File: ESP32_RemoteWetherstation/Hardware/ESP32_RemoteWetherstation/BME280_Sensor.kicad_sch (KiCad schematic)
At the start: 6 parts, among them U302 BME280

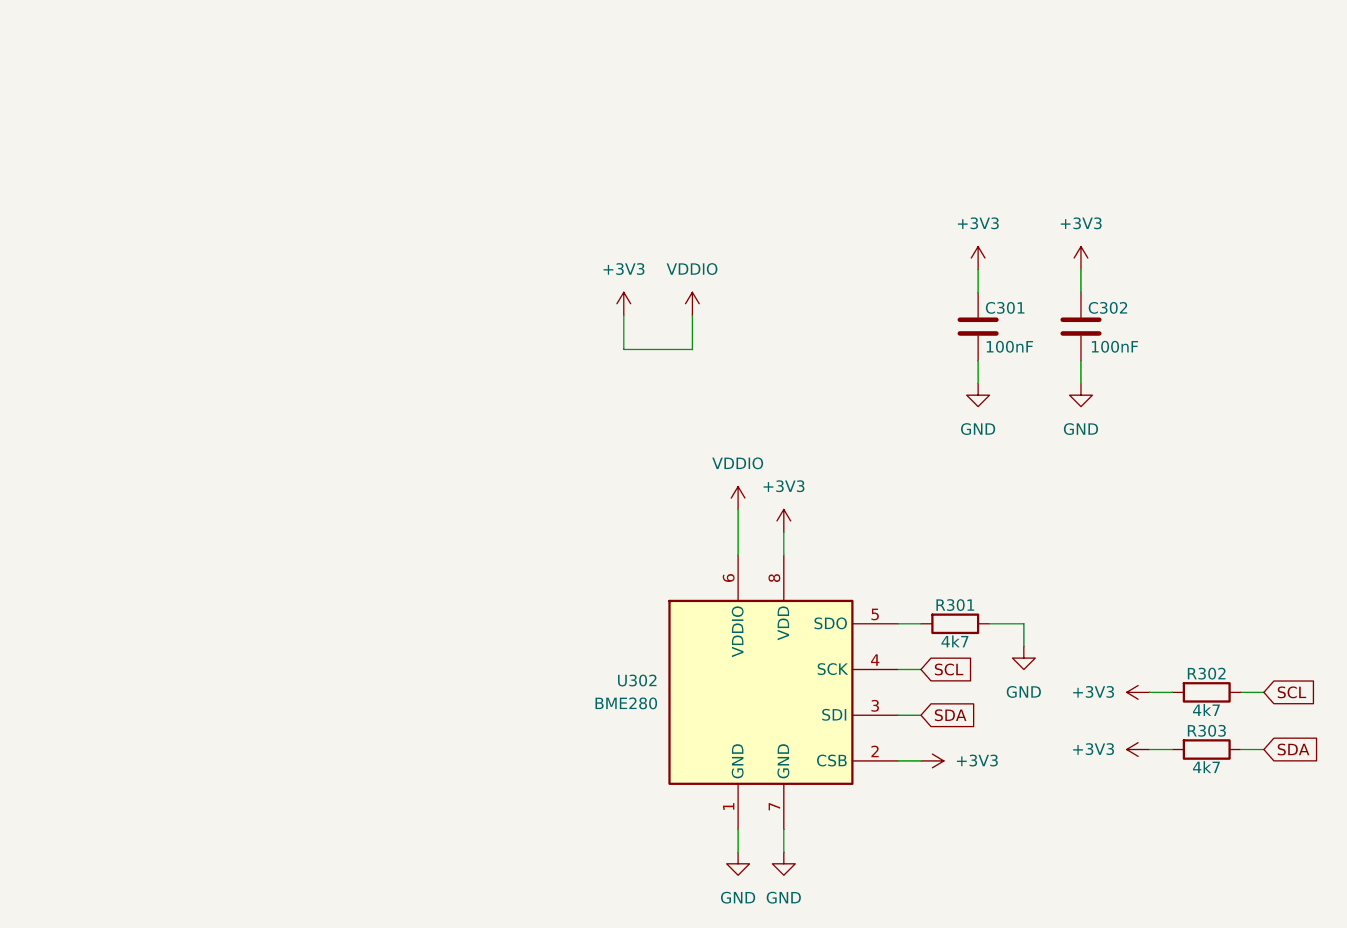
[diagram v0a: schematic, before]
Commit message: edited schematic looks
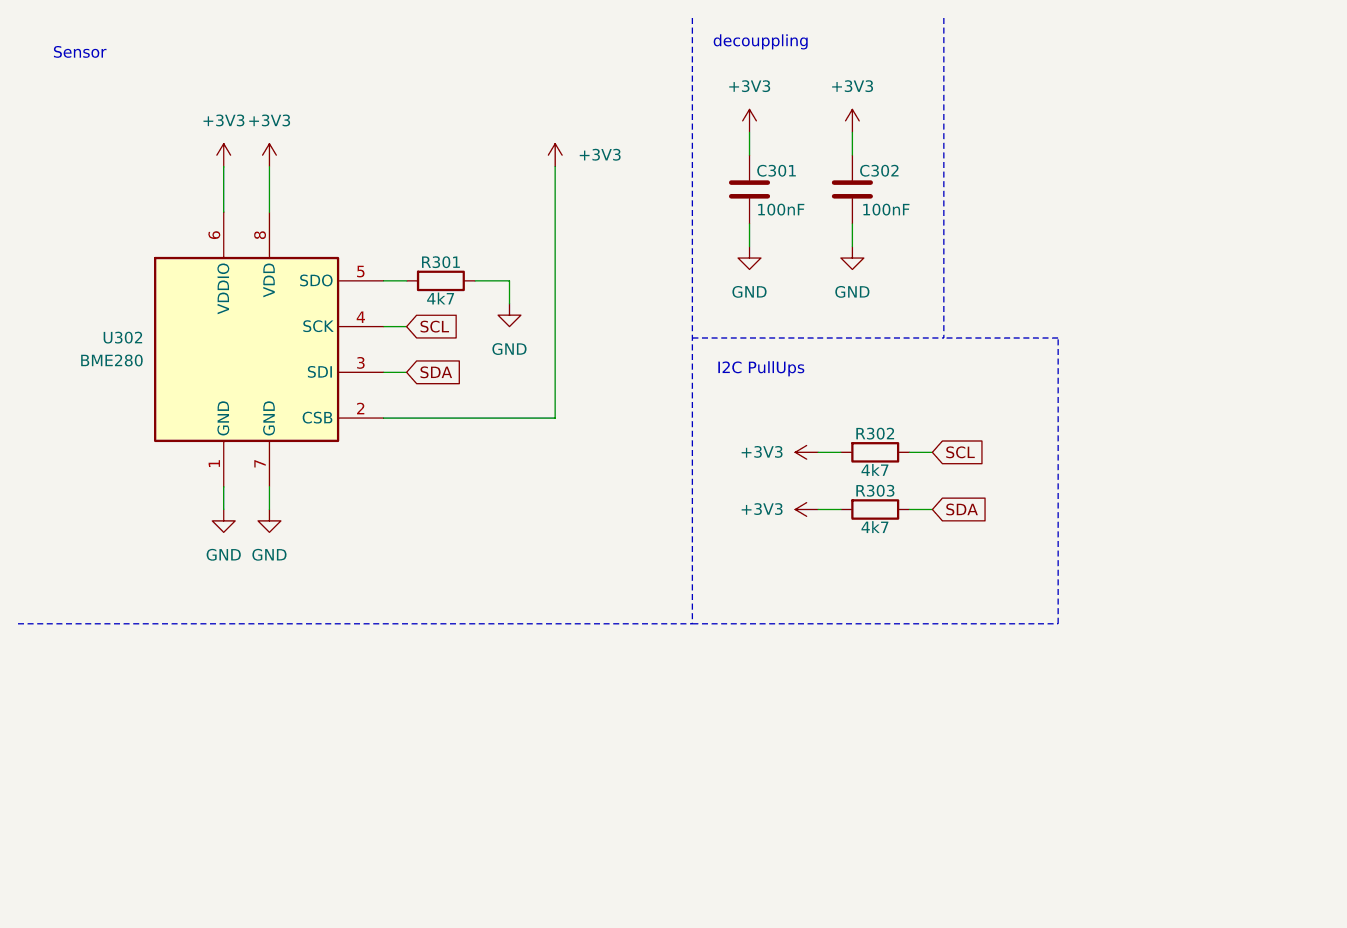
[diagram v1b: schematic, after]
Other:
- note added: "I2C PullUps"
- note added: "Sensor"
- note added: "decouppling"
- moved on the sheet: C301, C302, R301, R302, R303, U302

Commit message: changed MCU
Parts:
- C301, C302: footprint Capacitor_SMD:C_0603_1608Metric_Pad1.08x0.95mm_HandSolder -> Capacitor_SMD:C_0402_1005Metric
- R301, R302, R303: footprint Resistor_SMD:R_0603_1608Metric -> Resistor_SMD:R_0402_1005Metric
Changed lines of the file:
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@@
 			)
 		)
-		(property "Footprint" "Resistor_SMD:R_0603_1608Metric"
+		(property "Footprint" "Resistor_SMD:R_0402_1005Metric"
 			(at 59.69 40.132 90)
 			(effects
@@
 			)
 		)
-		(property "Footprint" "Capacitor_SMD:C_0603_1608Metric_Pad1.08x0.95mm_HandSolder"
+		(property "Footprint" "Capacitor_SMD:C_0402_1005Metric"
 			(at 106.3752 35.56 0)
 			(effects
@@
 			)
 		)
-		(property "Footprint" "Resistor_SMD:R_0603_1608Metric"
+		(property "Footprint" "Resistor_SMD:R_0402_1005Metric"
 			(at 107.95 59.182 90)
 			(effects
@@
 			)
 		)
-		(property "Footprint" "Resistor_SMD:R_0603_1608Metric"
+		(property "Footprint" "Resistor_SMD:R_0402_1005Metric"
 			(at 107.95 65.532 90)
 			(effects
@@
 			)
 		)
-		(property "Footprint" "Capacitor_SMD:C_0603_1608Metric_Pad1.08x0.95mm_HandSolder"
+		(property "Footprint" "Capacitor_SMD:C_0402_1005Metric"
 			(at 94.9452 35.56 0)
 			(effects
